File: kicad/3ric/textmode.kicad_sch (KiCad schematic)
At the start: 2 parts

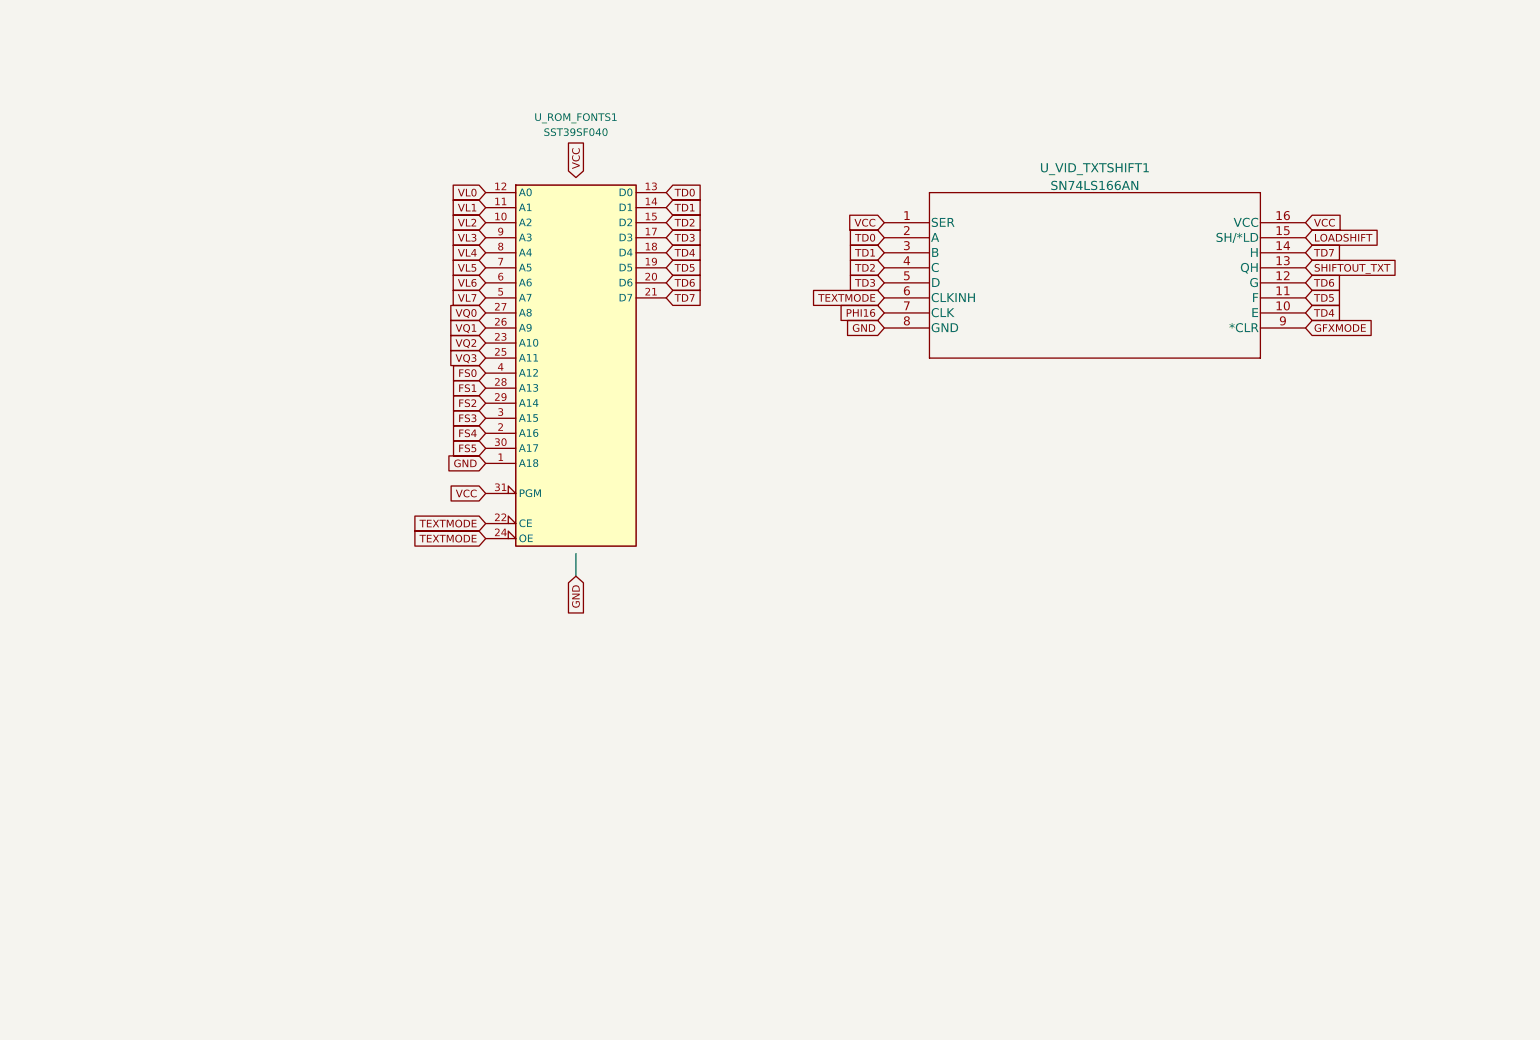
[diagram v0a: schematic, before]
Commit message: schematic updates - bring the schematics up to match breadboard changes current state has high res Apple II color emulation working
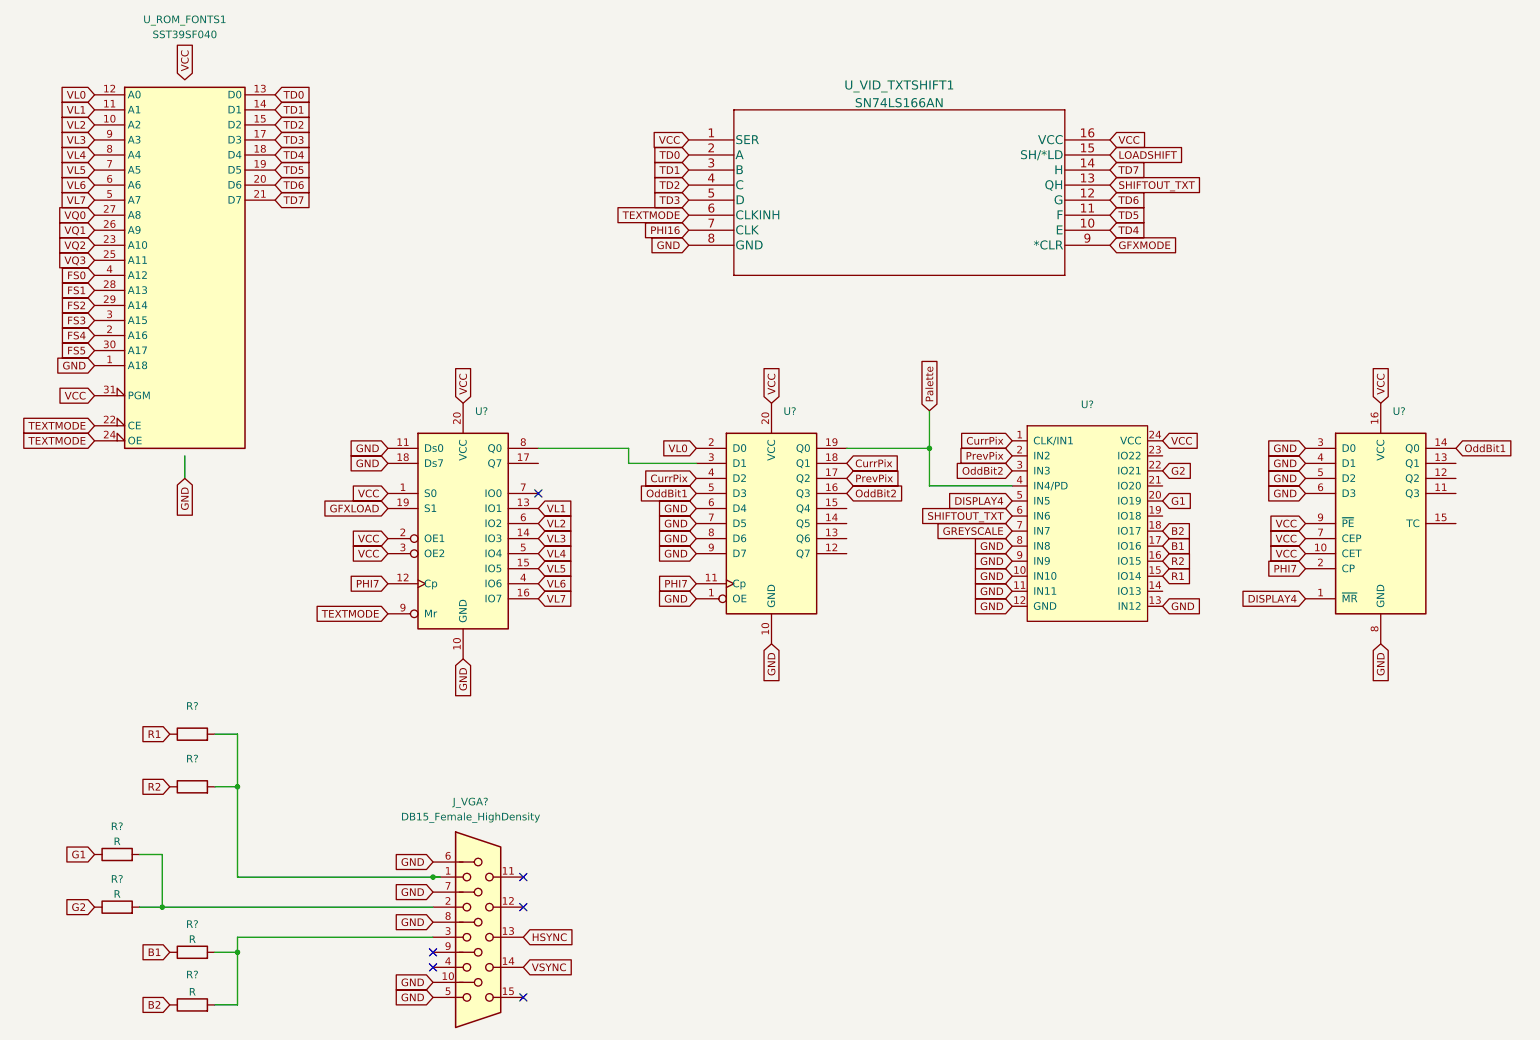
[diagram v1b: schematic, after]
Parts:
- added J_VGA?: DB15_Female_HighDensity, Connector_Dsub:DSUB-15-HD_Female_Horizontal_P2.29x1.98mm_EdgePinOffset8.35mm_Housed_MountingHolesOffset10.89mm, symbol Connector:DB15_Female_HighDensity
- added R? (x4): R, symbol Device:R
- added R? (x2): (no value), symbol Device:R
- added U?: (no value), symbol 6502:22V10C
- added U?: (no value), symbol 74xx:74LS161
- added U?: (no value), symbol 74xx:74LS574
- added U?: (no value), symbol 74xx:74LS299
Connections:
- net GND: now also J_VGA?.10, J_VGA?.5, J_VGA?.6, J_VGA?.7, J_VGA?.8, U?.1 (OE), U?.10 (GND), U?.10 (GND), U?.10 (IN10), U?.11 (Ds0), U?.11 (IN11), U?.12 (GND), U?.13 (IN12), U?.18 (Ds7), U?.3 (D0), U?.4 (D1), U?.5 (D2), U?.6 (D3), U?.6 (D4), U?.7 (D5), U?.8 (D6), U?.8 (GND), U?.8 (IN8), U?.9 (D7), U?.9 (IN9)
- net SHIFTOUT_TXT: now also U?.6 (IN6)
- net TEXTMODE: now also U?.9 (Mr)
- net VCC: now also U?.1 (S0), U?.10 (CET), U?.16 (VCC), U?.2 (OE1), U?.20 (VCC), U?.20 (VCC), U?.24 (VCC), U?.3 (OE2), U?.7 (CEP), U?.9 (~{PE})
- net VL0: now also U?.2 (D0)
- net VL1: now also U?.13 (IO1)
- net VL2: now also U?.6 (IO2)
- net VL3: now also U?.14 (IO3)
- net VL4: now also U?.5 (IO4)
- net VL5: now also U?.15 (IO5)
- net VL6: now also U?.4 (IO6)
- net VL7: now also U?.16 (IO7)
- new net: J_VGA?.3, R?.2, R?.2
- new net: J_VGA?.1, R?.2, R?.2
- new net: J_VGA?.2, R?.2, R?.2
- new net: U?.3 (D1), U?.8 (Q0)
- new net B1: R?.1, U?.17 (IO16)
- new net B2: R?.1, U?.18 (IO17)
- new net CurrPix: U?.1 (CLK/IN1), U?.18 (Q1), U?.4 (D2)
- new net DISPLAY4: U?.1 (~{MR}), U?.5 (IN5)
- new net G1: R?.1, U?.20 (IO19)
- new net G2: R?.1, U?.22 (IO21)
- new net GFXLOAD: U?.19 (S1)
- new net GREYSCALE: U?.7 (IN7)
- new net HSYNC: J_VGA?.13
- new net OddBit1: U?.14 (Q0), U?.5 (D3)
- new net OddBit2: U?.16 (Q3), U?.3 (IN3)
- new net PHI7: U?.11 (Cp), U?.12 (Cp), U?.2 (CP)
- new net Palette: U?.19 (Q0), U?.4 (IN4/PD)
- new net PrevPix: U?.17 (Q2), U?.2 (IN2)
- new net R1: R?.1, U?.15 (IO14)
- new net R2: R?.1, U?.16 (IO15)
- new net VSYNC: J_VGA?.14
- no-connect marks 0 -> 6
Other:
- moved on the sheet: U_ROM_FONTS1, U_VID_TXTSHIFT1
